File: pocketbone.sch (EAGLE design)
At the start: 60 parts, among them J1 USD_CONNECTOR, U1 24LC_32AT-I/OT, U2 OSD3358, U3 SN74LVC1G07_DCK_5, Y1 CM200C-32.768KAZF-UT, Y2 445C33D24M00000

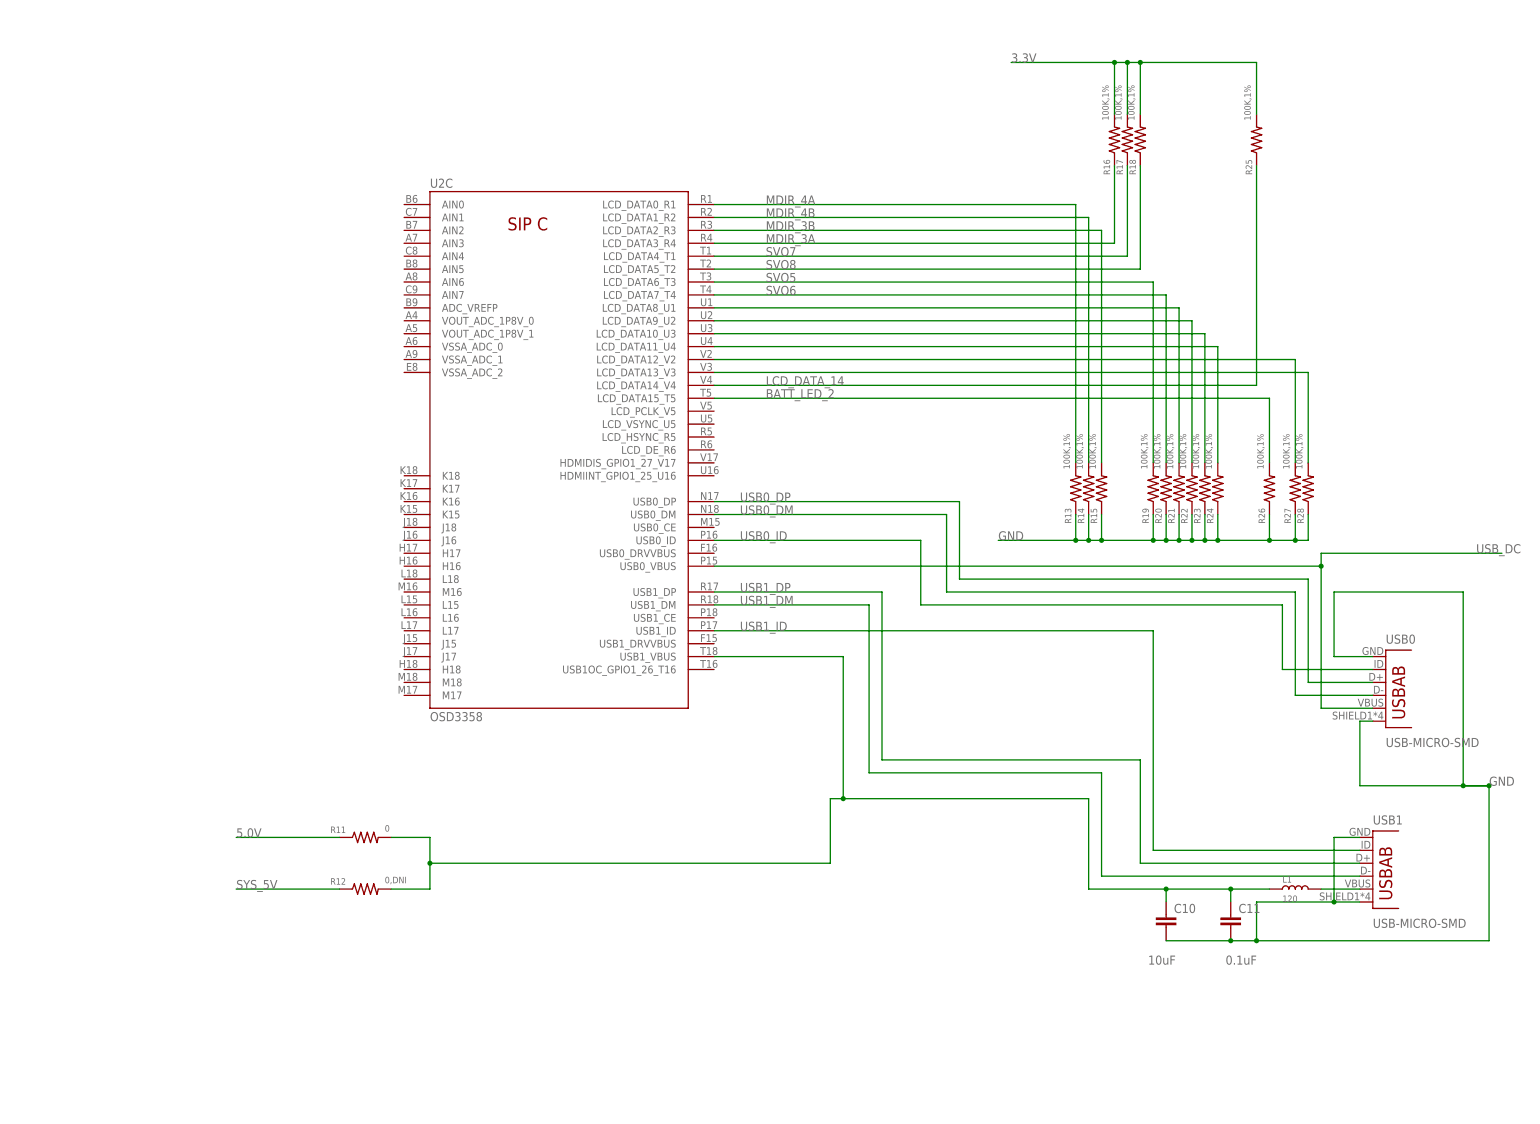
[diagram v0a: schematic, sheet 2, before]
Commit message: Updated components to match BB Blue.
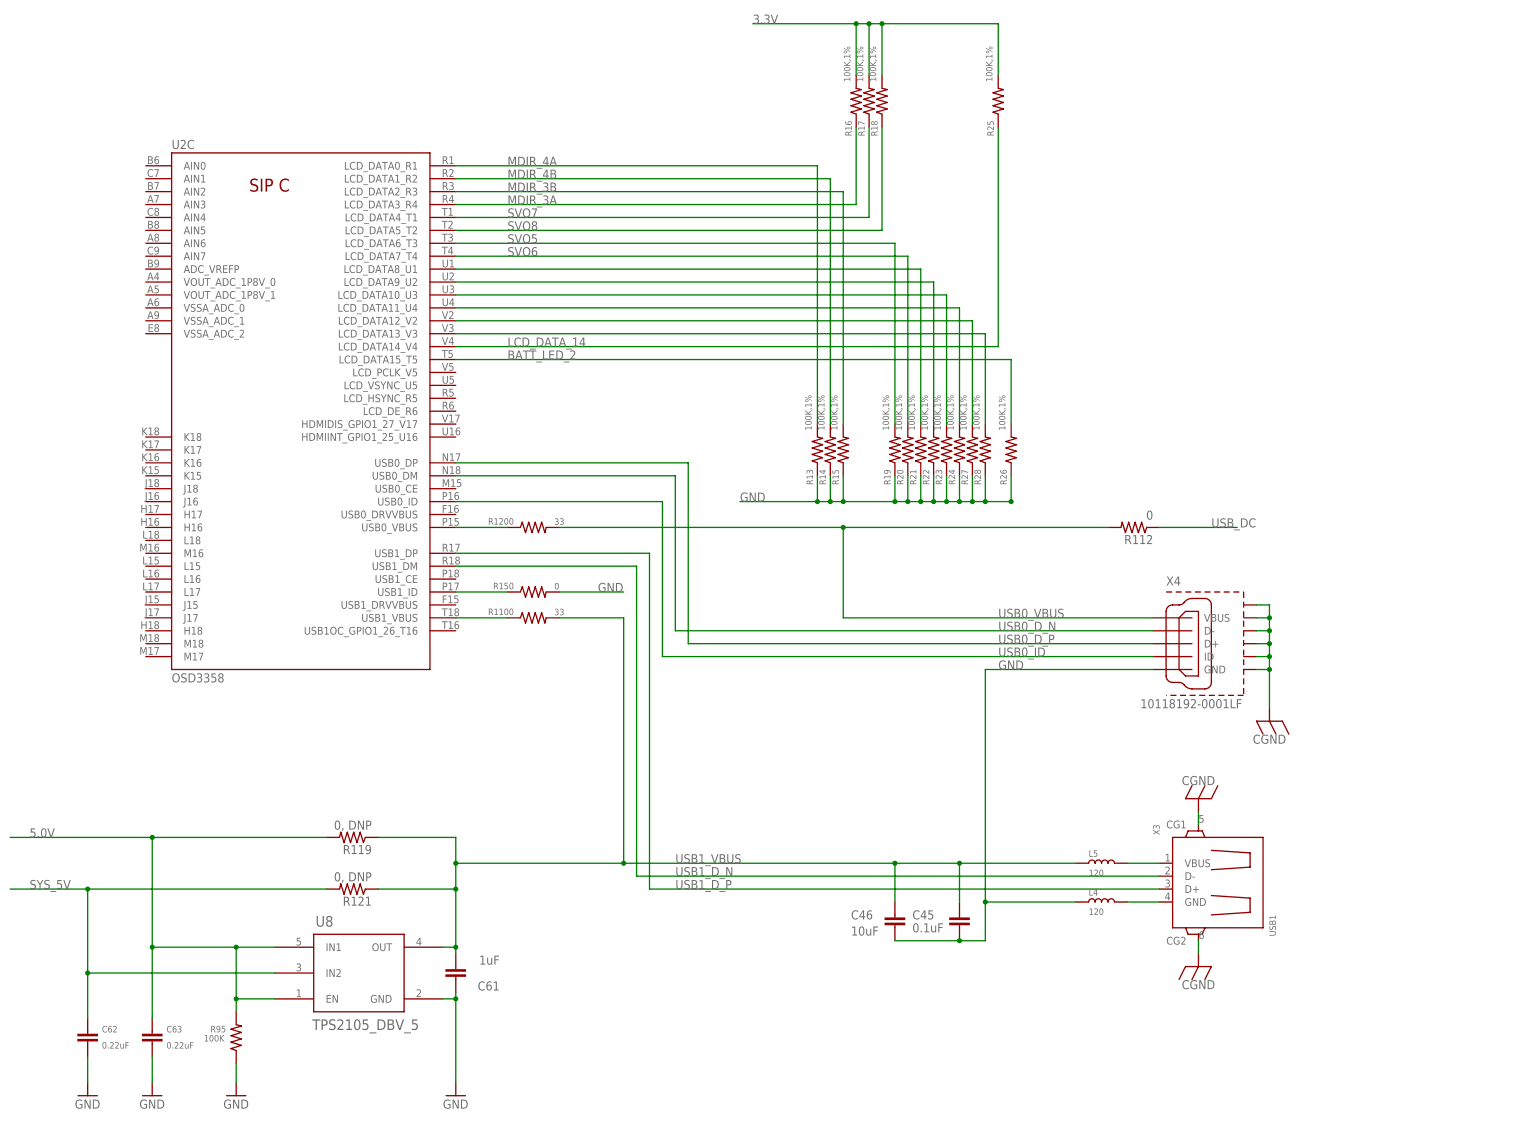
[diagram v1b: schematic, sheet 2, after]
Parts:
- removed C10, C2: 10uF, Strawson_Eagle_Lib:CAP0805
- removed C11, C3: 0.1uF, Strawson_Eagle_Lib:CAP0402-CAP
- removed C4, C5, C6, C7: 20pF, Strawson_Eagle_Lib:CAP0402-CAP
- removed J1: USD_CONNECTOR, pocketbone:USD_CONNECTOR
- removed L1: 120, Seeed-OPL-Inductor:INDUCTOR/FERRITE-BEAD'0603'
- removed TP1, TP2, TP3, TP4: TPSQPAD1-17, pocketbone:TPSQPAD1-17
- removed USB0, USB1: USB-MICRO-SMD, pocketbone:USB-AB
- removed Y2: 445C33D24M00000, pocketbone:445C33D24M00000
- added 5.0V, GND, WP, WPG: GHI_TESTPAD/W_HOLE_1X1, pocketbone:GHI_TESTPAD/W_HOLE_1X1
- added C29, C30: 10pF, Strawson_Eagle_Lib:CAP0402-CAP
- added C34, C46: 10uF, Strawson_Eagle_Lib:CAP0805
- added C35, C45: 0.1uF, Strawson_Eagle_Lib:CAP0402-CAP
- added C61: 1uF, Strawson_Eagle_Lib:CAP0402-CAP
- added C62, C63: 0.22uF, Strawson_Eagle_Lib:CAP0402-CAP
- added L4, L5: 120, Seeed-OPL-Inductor:INDUCTOR/FERRITE-BEAD'0603'
- added R1100, R1200: 33, Strawson_Eagle_Lib:RESISTOR0402-RES
- added R112: 0, SparkFun-Resistors:RESISTOR0603
- added R119, R121: 0, DNP, SparkFun-Resistors:RESISTOR0603
- added R150: 0, Strawson_Eagle_Lib:RESISTOR0402-RES
- added R32: 1M, Strawson_Eagle_Lib:RESISTOR0402-RES
- added R54, R55, R56, R57, R65: 10K, Strawson_Eagle_Lib:RESISTOR0402-RES
- added R95: 100K, Strawson_Eagle_Lib:RESISTOR0402-RES
- added SYS_5V: TPSQB1,27, testpad:TPSQB1,27
- added U8: TPS2105_DBV_5, BeagleBone_Blue:TPS2105_DBV_5
- added X2: SCHA5B0200, GHI-Connectors:SCHA5B0200(ALPS_USD)
- added X3: USB1, GHI2:USB_HOST_W/CHASSIS_GND
- added X4: 10118192-0001LF, GHI-Connectors:10118192-0001LF
- R11: value 0 -> 10K
- R12: value 0,DNI -> 10K
- R8, R9: value 4.87k -> 4.7k
- Y1: value CM200C-32.768KAZF-UT -> 24 MHz; device pocketbone:CM200C-32.768KAZF-UT -> GHI2:CRYSTAL_5X3.2MM
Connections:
- removed net N$129: C10.1, C11.1, L1.1, R11.2, R12.2, U2C.USB1_VBUS
- removed net N$2: J1.CLK, U2B.MMC0_CLK_G17
- removed net N$32: C6.1, U2B.OSC1_IN, Y2.2
- removed net N$33: C4.2, U2B.OSC1_OUT, Y2.1
- removed net N$34: C4.1, C6.2, U2B.OSC1_GND
- removed net N$5: J1.CD/DAT3, U2B.MMC0_DAT3_F17
- removed net N$70: J1.DAT1, U2B.MMC0_DAT1_G15
- removed net N$74: J1.CMD, U2B.MMC0_CMD_G18
- removed net N$75: J1.CD1, U2B.MMC0_CD_C15
- removed net N$77: J1.DAT0, U2B.MMC0_DAT0_G16
- removed net NTE: J1.DAT2, U2B.MMC0_DAT2_F18
- removed net USB0_DM: U2C.USB0_DM, USB0.D-
- removed net USB0_DP: U2C.USB0_DP, USB0.D+
- removed net USB1_DM: U2C.USB1_DM, USB1.D-
- removed net USB1_DP: U2C.USB1_DP, USB1.D+
- removed net USB1_ID: U2C.USB1_ID, USB1.USBID
- new net CGND: X2.CGND1, X2.CGND2, X2.CGND3, X2.CGND4, X2.CGND5, X2.CGND6, X3.CG1, X3.CG2, X4.SGND1, X4.SGND2, X4.SGND3, X4.SGND4, X4.SGND5, X4.SGND6
- new net N$11: R1100.1, U2C.USB1_VBUS
- new net N$126: R150.1, U2C.USB1_ID
- new net N$128: L4.2, X3.GND
- new net N$130: L5.2, X3.VBUS
- new net N$3: R56.1, U2B.MMC0_CMD_G18, X2.CMD/DI
- new net N$4: R55.1, U2B.MMC0_DAT0_G16, X2.DAT0/DO
- new net N$6: R54.1, U2B.MMC0_DAT1_G15, X2.DAT1
- new net N$7: R65.1, U2B.MMC0_CD_C15, X2.CD#
- new net N$8: R57.1, U2B.MMC0_CLK_G17, X2.CLK
- new net N$9: R11.1, U2B.MMC0_DAT3_F17, X2.DAT3/CS
- new net NTE1: R12.1, U2B.MMC0_DAT2_F18, X2.DAT2
- new net USB0_D_N: U2C.USB0_DM, X4.D-
- new net USB0_D_P: U2C.USB0_DP, X4.D+
- new net USB0_VBUS: R112.2, R1200.2, X4.VBUS
- new net USB1_D_N: U2C.USB1_DM, X3.D-
- new net USB1_D_P: U2C.USB1_DP, X3.D+
- new net USB1_VBUS: C45.1, C46.1, C61.2, L5.1, R1100.2, R119.1, R121.1, U8.OUT
- net 3.3V: now also C34.2, C35.2, R11.2, R12.2, R54.2, R55.2, R56.2, R57.2, R65.2, X2.VDD; no longer C2.2, C3.2, J1.VCC
- net 5.0V: now also 5.0V.TP, C63.1, R119.2, R95.2, U8.EN, U8.IN1; no longer R11.1, TP2.TP
- net GND: now also C34.1, C35.1, C45.2, C46.2, C61.1, C62.2, C63.2, GND.TP, L4.1, R150.2, R95.1, U8.GND, WPG.TP, X2.GND, X2.VSS, X4.GND; no longer C10.2, C11.2, C2.1, C3.1, J1.GND, J1.SHIELD@1, J1.SHIELD@3, TP3.TP, USB0.GND, USB0.SHIELD, USB1.GND, USB1.SHIELD
- net N$1: now also R1200.1, U2C.USB0_VBUS; no longer L1.2, USB1.VBUS
- net N$26: now also C30.1, R32.2, Y1.P$2; no longer C7.1, Y1.2
- net N$27: now also C29.1, R32.1, Y1.P$1; no longer C5.1, Y1.1
- net N$28: now also WP.TP; no longer TP4.TP
- net N$31: now also C29.2, C30.2; no longer C5.2, C7.2
- net SYS_5V: now also C62.1, R121.2, SYS_5V.TP, U8.IN2; no longer R12.1, TP1.TP
- net USB0_ID: now also X4.ID; no longer USB0.USBID
- net USB_DC: now also R112.1; no longer U2C.USB0_VBUS, USB0.VBUS
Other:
- moved on the sheet: C9, POWER, R1, R10, R13, R14, R15, R16, R17, R18, R19, R2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
